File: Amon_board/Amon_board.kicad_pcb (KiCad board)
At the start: 4 copper layers, 70 x 120 mm, 118 parts, among them J1 USB2.0_C_Rev, J10 GTFP08131Y2HR, J11 Conn_01x03_Male, J12 Conn_01x06_Male, J13 Conn_01x04_Male, J14 Conn_01x04_Male, J15 Conn_01x06_Male, J16 Conn_02x09_Odd_Even, J2 Conn_2x5 pin, J3 Switch_port, J4 XT60-F, J5 XT60-F, J6 Conn_02x04_Odd_Even, J7 Red leds, J8 White leds, J9 Conn_02x04_Odd_Even, M1 Servo_X+, M2 Servo_X-, M3 Servo_Y+, M4 Servo_Y-, Q1 BC817, Q2 BC817, SW1 SW_DPDT, SW2 SW_SPST, U1 USBLC6-2P6, U2 STM32F405RGT6-LQFP64, U3 W25Q128JVS, U4 MP2303ADN, U5 MP2303ADN, U6 MPU-6050, U7 BME280, Y1 25MHz

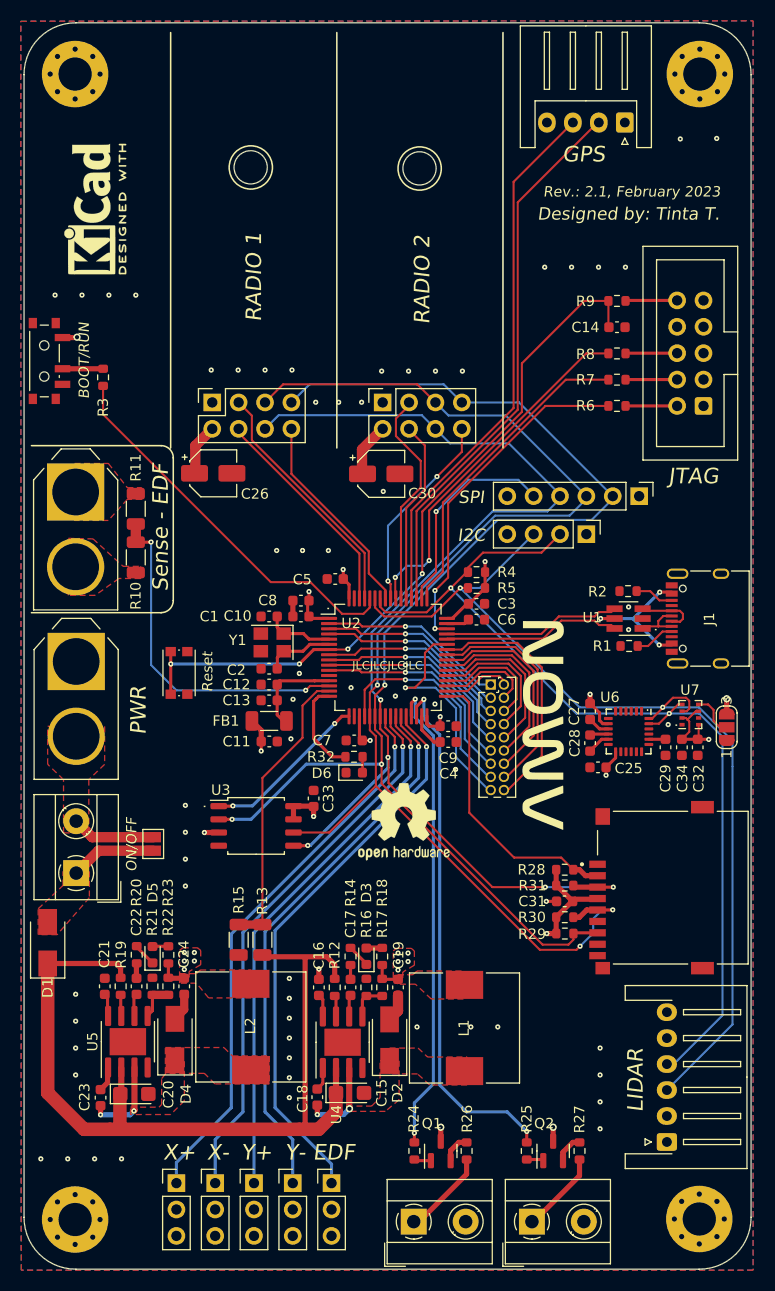
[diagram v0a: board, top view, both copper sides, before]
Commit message: PCB update, stl update (pcb holder)
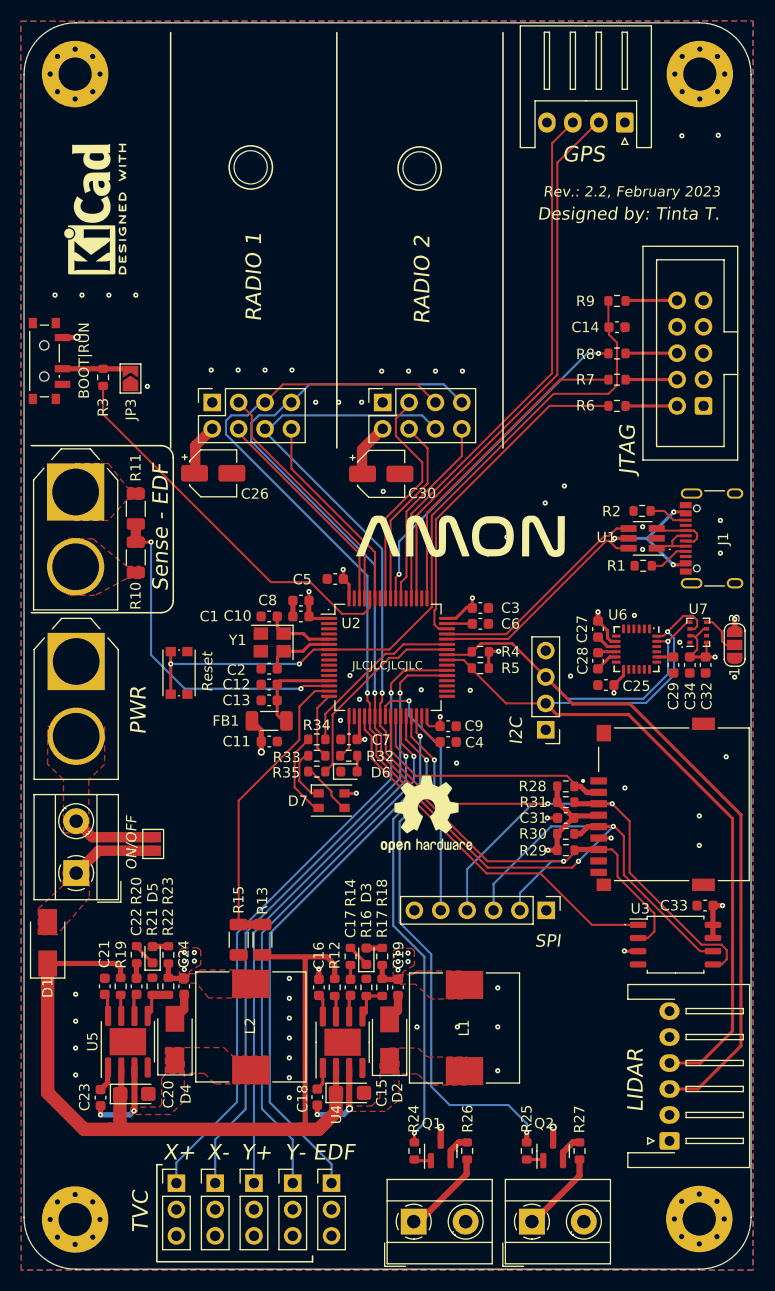
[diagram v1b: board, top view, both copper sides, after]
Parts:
- removed J16: Conn_02x09_Odd_Even, Connector_PinHeader_1.27mm:PinHeader_2x09_P1.27mm_Vertical
- added D7: LED_RGBA, LED_SMD:LED_Cree-PLCC4_3.2x2.8mm_CCW, F.Cu at (184.6, 103.9)
- added JP3: SolderJumper_2_Open, Jumper:SolderJumper-2_P1.3mm_Open_TrianglePad1.0x1.5mm, F.Cu at (165.3, 63.2)
- added R33: 330, Resistor_SMD:R_0603_1608Metric, F.Cu at (183.2, 99.6)
- added R34: 330, Resistor_SMD:R_0603_1608Metric, F.Cu at (183.2, 98.0)
- added R35: 330, Resistor_SMD:R_0603_1608Metric, F.Cu at (183.2, 101.1)
- moved U3 42.0 mm to (217.7, 117.8)
- moved J15 40.9 mm to (205.3, 114.5)
- moved C33 39.1 mm to (220.6, 114.0), turned to 0 degrees
- moved G*** 19.9 mm to (197.0, 78.4), turned to 0 degrees
- moved J14 19.2 mm to (205.2, 97.1), turned to 180 degrees
- moved C31 8.03 mm to (207.2, 105.6)
- moved R28 8.03 mm to (207.2, 102.5)
- moved R29 8.03 mm to (207.2, 108.7)
- moved R31 8.03 mm to (207.2, 104.0)
- moved J10 8.03 mm to (220.4, 104.2)
- moved R30 8.03 mm to (207.2, 107.1)
- moved C29 7.96 mm to (217.5, 90.8)
- moved C32 7.96 mm to (220.6, 90.8)
- moved C34 7.96 mm to (219.1, 90.8)
- moved U6 7.96 mm to (214.0, 89.3)
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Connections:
- J1 pad : GND -> (no net)
- J12 pad 3: SDA -> SCL
- J12 pad 4: SCL -> SDA
- J13 pad 2: RX_GPS -> TX_GPS
- J13 pad 3: TX_GPS -> RX_GPS
- J14 pad 2: SCL -> SDA
- J14 pad 3: SDA -> SCL
- U2 pad 10: PH11 -> unconnected-(U2-Pad10)
- U2 pad 11: PH13 -> unconnected-(U2-Pad11)
- U2 pad 16: Brd_Led -> RGB_Led_B
- U2 pad 17: CS_Flash -> Brd_Led
- U2 pad 2: PH1 -> unconnected-(U2-Pad2)
- U2 pad 20: PH15 -> CS_Flash
- U2 pad 24: PWM_Servo_X+ -> CS_EXT
- U2 pad 25: PWM_Servo_X- -> CS_SD
- U2 pad 28: PWM_EDF -> LED_Red
- U2 pad 29: LED_Red -> LED_White
- U2 pad 3: PH3 -> unconnected-(U2-Pad3)
- U2 pad 30: LED_White -> PWM_EDF
- U2 pad 33: CS_SD -> unconnected-(U2-Pad33)
- U2 pad 34: PH2 -> unconnected-(U2-Pad34)
- U2 pad 35: PH4 -> unconnected-(U2-Pad35)
- U2 pad 36: PH6 -> unconnected-(U2-Pad36)
- U2 pad 37: PH8 -> PWM_Servo_X-
- U2 pad 38: PH10 -> PWM_Servo_X+
- U2 pad 39: PH12 -> unconnected-(U2-Pad39)
- U2 pad 4: PH5 -> unconnected-(U2-Pad4)
- U2 pad 40: PH14 -> SDA
- U2 pad 41: PH16 -> SCL
- U2 pad 42: PH18 -> RGB_Led_G
- U2 pad 43: PH17 -> RGB_Led_R
- U2 pad 50: CS_EXT -> unconnected-(U2-Pad50)
- U2 pad 51: RX_GPS -> TX_GPS
- U2 pad 52: TX_GPS -> RX_GPS
- U2 pad 53: CS_RF2 -> unconnected-(U2-Pad53)
- U2 pad 54: EN_RF2 -> RF_IRQ2
- U2 pad 56: RF_IRQ2 -> CS_RF2
- U2 pad 57: RF_IRQ1 -> EN_RF2
- U2 pad 58: SCL -> unconnected-(U2-Pad58)
- U2 pad 59: SDA -> RF_IRQ1
- U2 pad 8: PH7 -> unconnected-(U2-Pad8)
- U2 pad 9: PH9 -> unconnected-(U2-Pad9)
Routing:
- net PH18: track 23.9 -> 0.00 mm
- net PH17: track 22.2 -> 0.00 mm, vias 1 -> 0
- net PH16: track 21.8 -> 0.00 mm
- net PH15: track 21.4 -> 0.00 mm, vias 1 -> 0
- net PH13: track 21.2 -> 0.00 mm, vias 1 -> 0
- net PH11: track 20.6 -> 0.00 mm, vias 1 -> 0
- net CS_Flash: track 16.1 -> 36.6 mm, vias 2 -> 0
- net PH9: track 20.0 -> 0.00 mm, vias 1 -> 0
- net PH14: track 19.6 -> 0.00 mm
- net MISO: track 124.8 -> 105.3 mm, vias 3 -> 2
- net PH7: track 19.5 -> 0.00 mm, vias 1 -> 0
- net RGB_Led_G: track 0.00 -> 19.4 mm
- net PH5: track 19.0 -> 0.00 mm, vias 1 -> 0
- net PH3: track 18.3 -> 0.00 mm, vias 1 -> 0
- net PH1: track 18.0 -> 0.00 mm, vias 1 -> 0
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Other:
- board text added: "BOOT|RUN"
- board text added: "Rev.: 2.2, February 2023"
- board text added: "TVC"
- board text removed: "BOOT/RUN"
- board text removed: "PH1 PH3 PH5 PH7 PH9 PH11 PH13 PH15 PH17"
- board text removed: "PH2 PH4 PH6 PH8 PH10 PH12 PH14 PH16 PH18"
- board text removed: "Rev.: 2.1, February 2023"

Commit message: updated stl, data, board update
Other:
- board text added: "SWDIO"
- board text removed: "IO"
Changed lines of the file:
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@@
     (effects (font (size 1 1) (thickness 0.2) italic) (justify mirror))
   )
-  (gr_text "IO" (at 215.947524 65.9892) (layer "B.SilkS")
+  (gr_text "SWDIO" (at 214.3252 65.9892) (layer "B.SilkS")
     (effects (font (size 1 1) (thickness 0.2) italic) (justify mirror))
   )

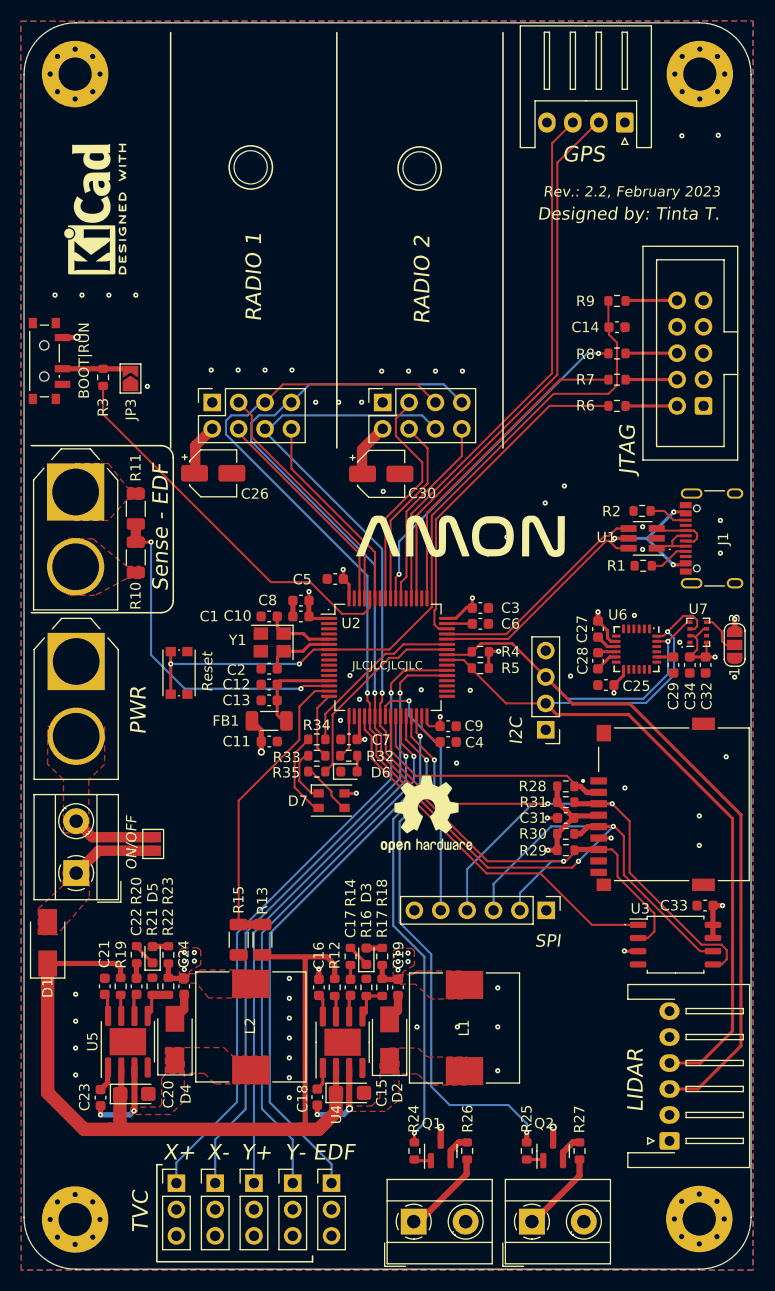
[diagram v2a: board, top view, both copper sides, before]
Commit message: PCB repair: crystal footprint, radio connector fliped, text
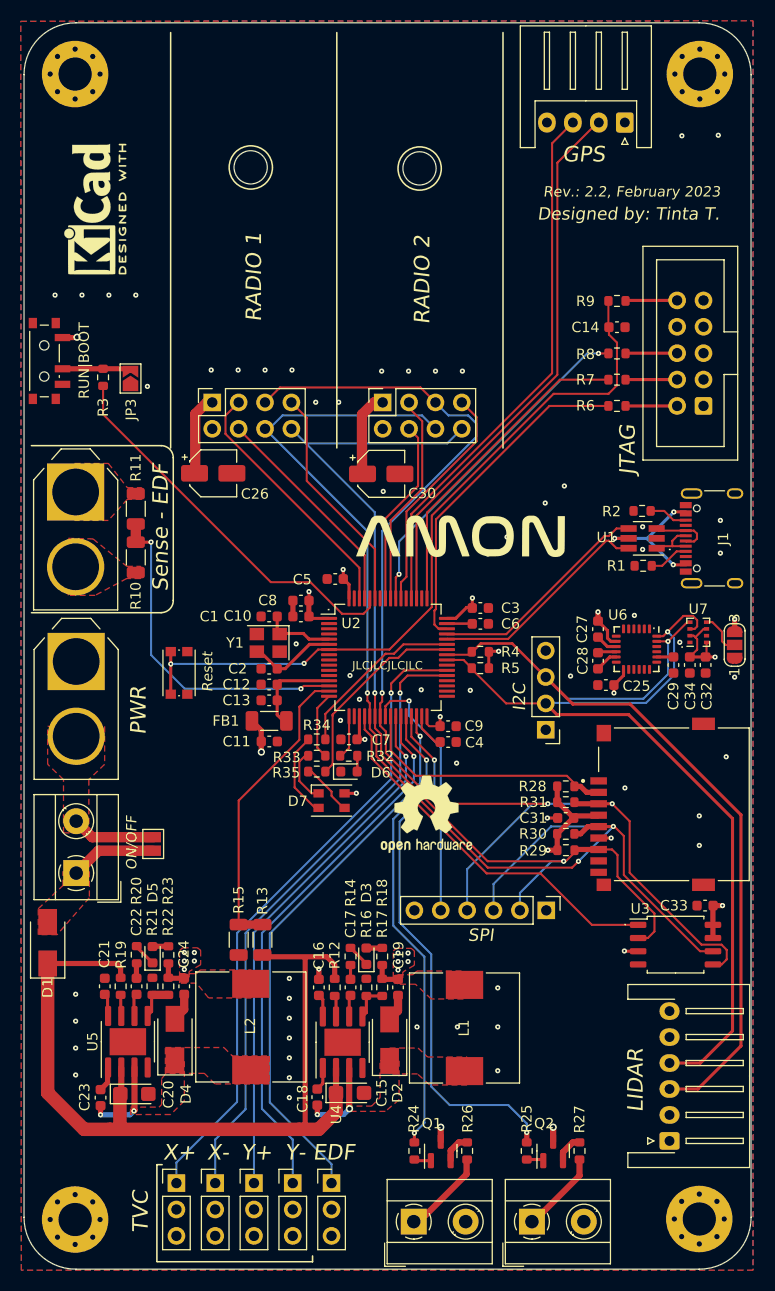
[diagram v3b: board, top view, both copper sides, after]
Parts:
- moved Y1 0.39 mm to (178.5, 88.7)
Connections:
- J1 pad S1: GND -> unconnected-(J1-PadS1)
- J6 pad 1: GND -> +3V3
- J6 pad 2: +3V3 -> GND
- J6 pad 3: EN_RF1 -> CS_RF1
- J6 pad 4: CS_RF1 -> EN_RF1
- J6 pad 5: CLK -> MOSI
- J6 pad 6: MOSI -> CLK
- J6 pad 7: MISO -> RF_IRQ1
- J6 pad 8: RF_IRQ1 -> MISO
- J9 pad 1: GND -> +3V3
- J9 pad 2: +3V3 -> GND
- J9 pad 3: EN_RF2 -> CS_RF2
- J9 pad 4: CS_RF2 -> EN_RF2
- J9 pad 5: CLK -> MOSI
- J9 pad 6: MOSI -> CLK
- J9 pad 7: MISO -> RF_IRQ2
- J9 pad 8: RF_IRQ2 -> MISO
- Y1 pad 3: GND -> /HSE_OUT
- Y1 pad 4: /HSE_OUT -> GND
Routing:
- net MISO: track 105.3 -> 96.2 mm
- net CLK: track 126.7 -> 119.5 mm
- net +3V3: track 72.5 -> 78.4 mm
- net MOSI: track 117.7 -> 122.3 mm
- net EN_RF2: track 21.9 -> 18.0 mm
- net RF_IRQ2: track 18.8 -> 22.5 mm
- net CS_RF1: track 21.1 -> 24.7 mm
- net RF_IRQ1: track 19.7 -> 22.2 mm
- net EN_RF1: track 23.9 -> 21.4 mm
- net /HSE_OUT: track 6.57 -> 8.78 mm
- net CS_RF2: track 18.5 -> 20.1 mm
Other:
- board text added: "RUN|BOOT"
- board text removed: "BOOT|RUN"

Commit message: changed directories
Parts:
- added C35: 4.7uF, Capacitor_SMD:C_0603_1608Metric, F.Cu at (205.7, 82.5)
- added C36: 0.22uF, Capacitor_SMD:C_0603_1608Metric, F.Cu at (204.1, 82.5)
- added C37: 100nF, Capacitor_SMD:C_0603_1608Metric, F.Cu at (215.0, 75.8)
- added R36: 22, Resistor_SMD:R_0603_1608Metric, F.Cu at (215.0, 77.3)
- added R37: 22, Resistor_SMD:R_0603_1608Metric, F.Cu at (215.0, 78.9)
- added U8: HMC5883L, HMC5883L:LPCC-16, F.Cu at (208.5, 82.6)
- C19, C24: footprint Capacitor_SMD:C_0603_1608Metric -> Capacitor_SMD:C_1206_3216Metric
- J4, J5: footprint XT60-M:AMASS_XT60-M -> XT60:AMASS_XT60-M
- moved C24 7.44 mm to (177.1, 118.5), turned to 180 degrees
- moved C19 7.38 mm to (197.6, 118.6), turned to 180 degrees
- moved U1 6.75 mm to (207.8, 78.3)
- moved G*** 5.65 mm to (191.4, 77.6)
- moved R13 3.65 mm to (177.1, 113.7), turned to 180 degrees
- moved R2 1.90 mm to (215.0, 74.2)
- moved R15 1.90 mm to (177.1, 116.0), turned to 0 degrees
- moved R1 0.87 mm to (215.0, 80.5)
- moved C23 0.09 mm to (162.5, 132.5)
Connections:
- J1 pad A6: /IN_D+ -> Net-(J1-D+-PadA6)
- J1 pad A7: /IN_D- -> Net-(J1-D--PadA7)
- J1 pad B6: /IN_D+ -> Net-(J1-D+-PadA6)
- J1 pad B7: /IN_D- -> Net-(J1-D--PadA7)
- R33 pad 1: RGB_Led_B -> RGB_Led_R
- R34 pad 1: RGB_Led_R -> RGB_Led_G
- R35 pad 1: RGB_Led_G -> RGB_Led_B
- U1 pad 1: /IN_D- -> /IN_D+
- U1 pad 3: /IN_D+ -> /IN_D-
- U1 pad 4: /USB_D+ -> /USB_D-
- U1 pad 6: /USB_D- -> /USB_D+
- U2 pad 16: RGB_Led_B -> RGB_Led_R
- U2 pad 42: RGB_Led_G -> RGB_Led_B
- U2 pad 43: RGB_Led_R -> RGB_Led_G
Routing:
- net RGB_Led_B: track 6.51 -> 19.5 mm
- net SCL: track 87.2 -> 98.6 mm, vias 1 -> 2
- net RGB_Led_R: track 16.9 -> 6.51 mm
- net VBUS: track 14.0 -> 24.4 mm
- net SDA: track 86.8 -> 96.7 mm
- net Net-(J1-D--PadA7): track 0.00 -> 7.91 mm, vias 0 -> 2
- net +3V3: track 78.4 -> 84.9 mm, vias 23 -> 26
- net Net-(J1-D+-PadA6): track 0.00 -> 5.90 mm
- net Net-(U8-SETP): track 0.00 -> 4.27 mm
- net /USB_D+: track 21.7 -> 17.8 mm
- net /Power/12V: track 86.0 -> 89.9 mm
- net Net-(U8-SETC): track 0.00 -> 3.84 mm
- net +5V: track 2.93 -> 5.72 mm, vias 5 -> 6
- net RGB_Led_G: track 19.4 -> 16.9 mm
- net BAT_BRD_S: track 29.2 -> 27.1 mm
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
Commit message: added pictires
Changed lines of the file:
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@@
   (segment (start 161.5652 107.412) (end 160.02 105.8668) (width 1) (layer "F.Cu") (net 14))
   (segment (start 167.4368 107.412) (end 161.5652 107.412) (width 1) (layer "F.Cu") (net 14))
+  (segment (start 205.232 78.1304) (end 205.3844 78.2828) (width 0.3) (layer "F.Cu") (net 15))
+  (segment (start 205.232 76.3524) (end 205.232 78.1304) (width 0.3) (layer "F.Cu") (net 15))
   (segment (start 217.5058 81.1784) (end 217.5158 81.1884) (width 0.3) (layer "F.Cu") (net 15))
   (segment (start 213.3219 75.7555) (end 213.3092 75.7428) (width 0.3) (layer "F.Cu") (net 15))
-  (segment (start 205.232 76.3524) (end 205.232 77.8764) (width 0.3) (layer "F.Cu") (net 15))
-  (segment (start 205.232 77.8764) (end 205.6384 78.2828) (width 0.3) (layer "F.Cu") (net 15))
   (segment (start 217.5566 76.0984) (end 217.5666 76.0884) (width 0.3) (layer "F.Cu") (net 15))
-  (segment (start 213.3092 75.7428) (end 213.2965 75.7555) (width 0.3) (layer "F.Cu") (net 15))
+  (segment (start 205.3844 78.2828) (end 206.4728 78.2828) (width 0.3) (layer "F.Cu") (net 15))
   (segment (start 214.2614 75.7555) (end 213.3219 75.7555) (width 0.3) (layer "F.Cu") (net 15))
   (segment (start 217.5158 81.1884) (end 218.7126 81.1884) (width 0.3) (layer "F.Cu") (net 15))
+  (segment (start 213.3092 75.7428) (end 213.2965 75.7555) (width 0.3) (layer "F.Cu") (net 15))
   (segment (start 217.5666 76.0884) (end 218.7126 76.0884) (width 0.3) (layer "F.Cu") (net 15))
-  (segment (start 205.6384 78.2828) (end 206.4728 78.2828) (width 0.3) (layer "F.Cu") (net 15))
   (segment (start 213.2965 75.7555) (end 205.8289 75.7555) (width 0.3) (layer "F.Cu") (net 15))
   (segment (start 205.8289 75.7555) (end 205.232 76.3524) (width 0.3) (layer "F.Cu") (net 15))
